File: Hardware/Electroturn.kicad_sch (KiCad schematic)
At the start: 31 parts, among them J1 Encoder Terminal, J2 Stepper Motor Terminal, SW1 Feed Switch, SW2 Motor Braking Switch, SW3 Mode Right Scroll, SW4 Mode Left Scroll, SW5 Function Btn 1, SW6 Function Btn 2, SW7 Function Btn 2, SW8 Control Panel Encoder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

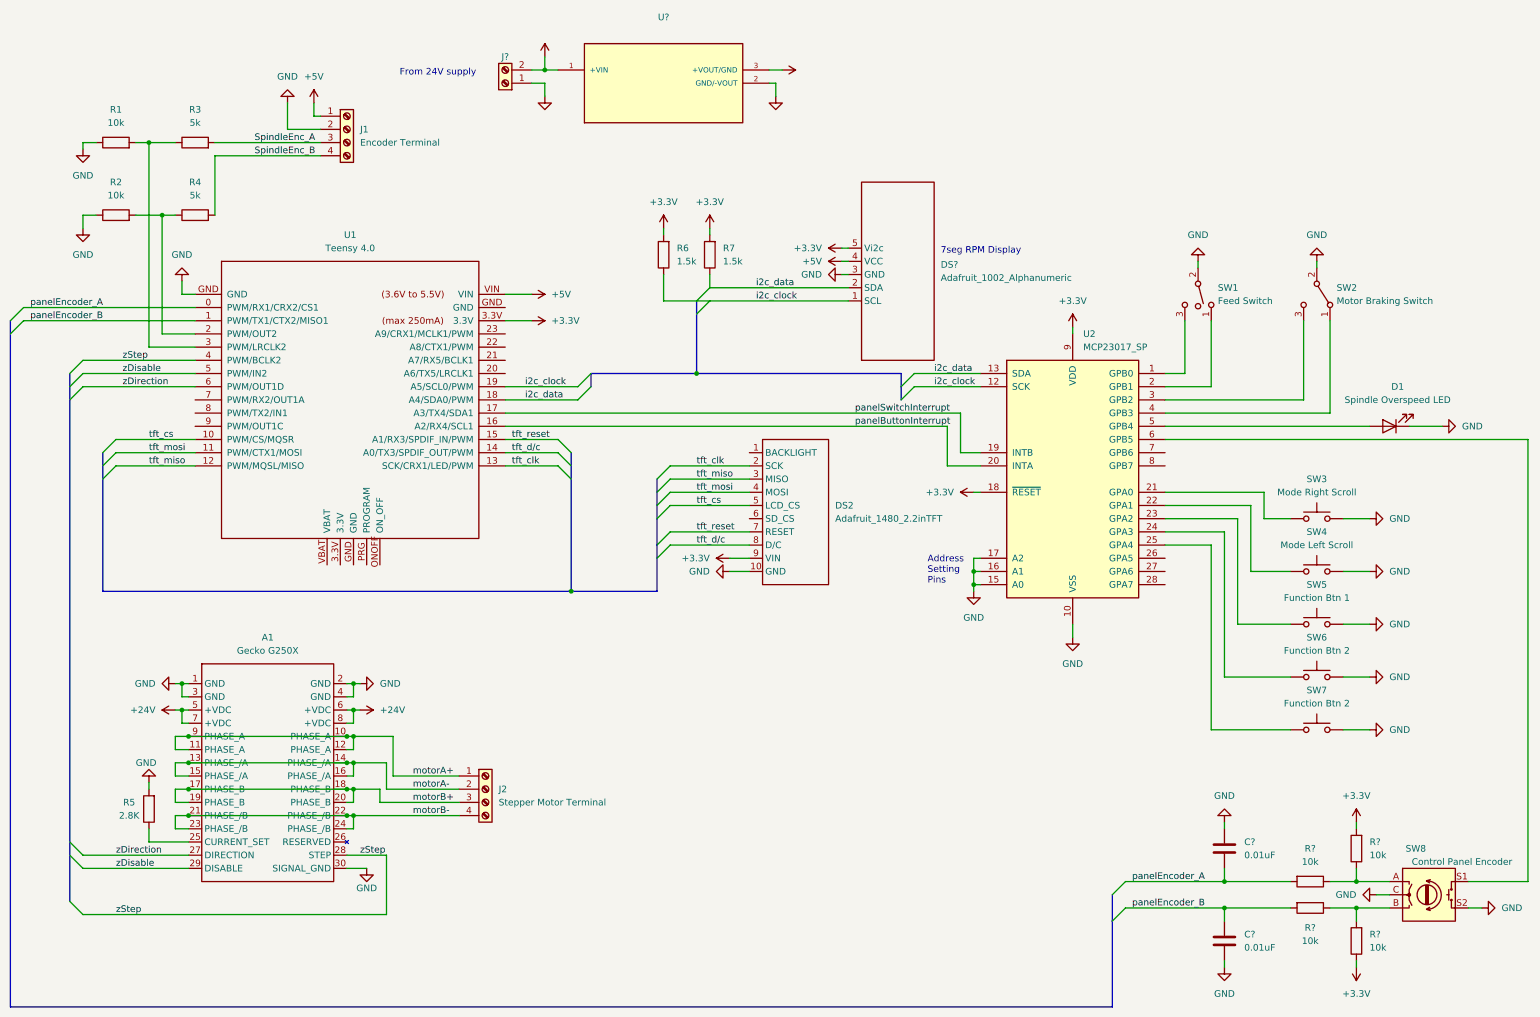
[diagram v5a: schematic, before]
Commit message: Footprint housekeeping, updating PCB components
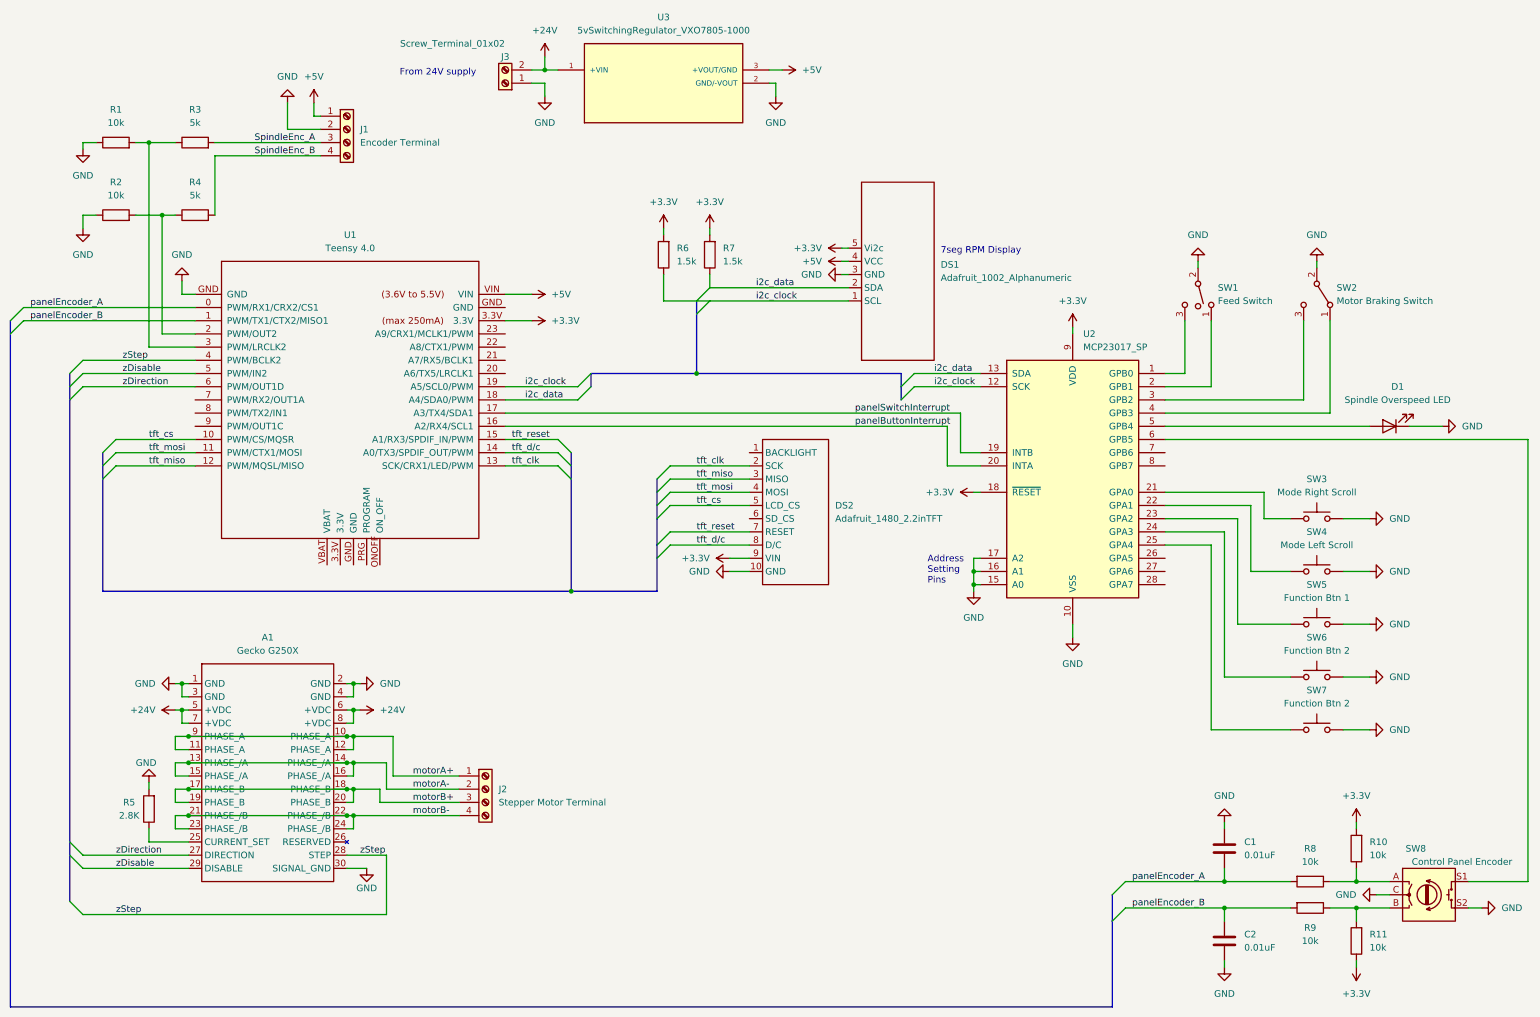
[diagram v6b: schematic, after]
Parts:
- J3: renamed from J?; value (none) -> Screw_Terminal_01x02
- U3: renamed from U?; value (none) -> 5vSwitchingRegulator_VXO7805-1000
- gave numbers to parts that had none: 7

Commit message: Some placement work
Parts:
- C1, C2: footprint (none) -> Capacitor_THT:C_Disc_D6.0mm_W2.5mm_P5.00mm
- D1: footprint (none) -> LED_THT:LED_D5.0mm
- DS1: footprint (none) -> Electroturn_Parts:Adafruit1002_0.54inAlphanumericBackpack
- DS2: footprint (none) -> Electroturn_Parts:Adafruit1480_TFTwithHeaders
- J3: footprint (none) -> Electroturn_Parts:01x02ScrewTerm_OSTVN02A150
- R10, R11, R6, R7, R8, R9: footprint (none) -> Resistor_THT:R_Axial_DIN0411_L9.9mm_D3.6mm_P12.70mm_Horizontal
- SW1: footprint (none) -> Electroturn_Parts:SPDT_OnOffOn_ToggleSwitch_fromECEdepartment_CircularPads
- SW2: footprint (none) -> Electroturn_Parts:SW_SPDT_CK_ A11405RNZQ
- SW3, SW4, SW5, SW6: footprint (none) -> Button_Switch_THT:SW_PUSH_6mm_H9.5mm
- SW7: value Function Btn 2 -> (none); footprint (none) -> Button_Switch_THT:SW_PUSH_6mm_H9.5mm
- SW8: footprint (none) -> Electroturn_Parts:CUIDevices_ACZ11BR1E20FD112C
- U3: footprint (none) -> Electroturn_Parts:5vSwitchingRegulator_CONV_VXO7805-1000
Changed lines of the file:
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@@
     (property "Reference" "SW3" (id 0) (at 303.53 109.22 0))
     (property "Value" "Mode Right Scroll" (id 1) (at 303.53 111.76 0))
-    (property "Footprint" "" (id 2) (at 303.53 111.76 0)
+    (property "Footprint" "Button_Switch_THT:SW_PUSH_6mm_H9.5mm" (id 2) (at 303.53 111.76 0)
       (effects (font (size 1.27 1.27)) hide)
     )
@@
     (property "Reference" "R8" (id 0) (at 302.26 180.34 90))
     (property "Value" "10k" (id 1) (at 302.26 182.88 90))
-    (property "Footprint" "" (id 2) (at 302.26 184.912 90)
+    (property "Footprint" "Resistor_THT:R_Axial_DIN0411_L9.9mm_D3.6mm_P12.70mm_Horizontal" (id 2) (at 302.26 184.912 90)
       (effects (font (size 1.27 1.27)) hide)
     )
@@
     (property "Reference" "SW5" (id 0) (at 303.53 129.54 0))
     (property "Value" "Function Btn 1" (id 1) (at 303.53 132.08 0))
-    (property "Footprint" "" (id 2) (at 303.53 132.08 0)
+    (property "Footprint" "Button_Switch_THT:SW_PUSH_6mm_H9.5mm" (id 2) (at 303.53 132.08 0)
       (effects (font (size 1.27 1.27)) hide)
     )
@@
     (property "Reference" "R9" (id 0) (at 302.26 195.58 90))
     (property "Value" "10k" (id 1) (at 302.26 198.12 90))
-    (property "Footprint" "" (id 2) (at 302.26 189.992 90)
+    (property "Footprint" "Resistor_THT:R_Axial_DIN0411_L9.9mm_D3.6mm_P12.70mm_Horizontal" (id 2) (at 302.26 189.992 90)
       (effects (font (size 1.27 1.27)) hide)
     )
@@
     (property "Reference" "J3" (id 0) (at 147.32 27.94 0))
     (property "Value" "Screw_Terminal_01x02" (id 1) (at 137.16 25.4 0))
-    (property "Footprint" "" (id 2) (at 147.32 33.02 0)
+    (property "Footprint" "Electroturn_Parts:01x02ScrewTerm_OSTVN02A150" (id 2) (at 147.32 33.02 0)
       (effects (font (size 1.27 1.27)) hide)
     )
@@
     (property "Reference" "SW4" (id 0) (at 303.53 119.38 0))
     (property "Value" "Mode Left Scroll" (id 1) (at 303.53 121.92 0))
-    (property "Footprint" "" (id 2) (at 303.53 121.92 0)
+    (property "Footprint" "Button_Switch_THT:SW_PUSH_6mm_H9.5mm" (id 2) (at 303.53 121.92 0)
       (effects (font (size 1.27 1.27)) hide)
     )
@@
       (effects (font (size 1.27 1.27)) (justify left))
     )
-    (property "Footprint" "" (id 2) (at 286.7152 184.15 0)
+    (property "Footprint" "Capacitor_THT:C_Disc_D6.0mm_W2.5mm_P5.00mm" (id 2) (at 286.7152 184.15 0)
       (effects (font (size 1.27 1.27)) hide)
     )
@@
     (property "Reference" "SW6" (id 0) (at 303.53 139.7 0))
     (property "Value" "Function Btn 2" (id 1) (at 303.53 142.24 0))
-    (property "Footprint" "" (id 2) (at 303.53 142.24 0)
+    (property "Footprint" "Button_Switch_THT:SW_PUSH_6mm_H9.5mm" (id 2) (at 303.53 142.24 0)
       (effects (font (size 1.27 1.27)) hide)
     )
@@
       (effects (font (size 1.27 1.27)) (justify left))
     )
-    (property "Footprint" "" (id 2) (at 303.53 73.66 0)
+    (property "Footprint" "Electroturn_Parts:SW_SPDT_CK_ A11405RNZQ" (id 2) (at 303.53 73.66 0)
       (effects (font (size 1.27 1.27)) hide)
     )
@@
       (effects (font (size 1.27 1.27)) (justify right))
     )
-    (property "Footprint" "" (id 2) (at 312.928 198.12 90)
+    (property "Footprint" "Resistor_THT:R_Axial_DIN0411_L9.9mm_D3.6mm_P12.70mm_Horizontal" (id 2) (at 312.928 198.12 90)
       (effects (font (size 1.27 1.27)) hide)
     )
@@
       (effects (font (size 1.27 1.27)) (justify left))
     )
-    (property "Footprint" "" (id 2) (at 210.82 134.62 0)
+    (property "Footprint" "Electroturn_Parts:Adafruit1480_TFTwithHeaders" (id 2) (at 210.82 134.62 0)
       (effects (font (size 1.27 1.27)) hide)
     )
@@
       (effects (font (size 1.27 1.27)) (justify left))
     )
-    (property "Footprint" "" (id 2) (at 286.7152 201.93 0)
+    (property "Footprint" "Capacitor_THT:C_Disc_D6.0mm_W2.5mm_P5.00mm" (id 2) (at 286.7152 201.93 0)
       (effects (font (size 1.27 1.27)) hide)
     )
@@
     (property "Reference" "SW8" (id 0) (at 322.58 180.34 0))
     (property "Value" "Control Panel Encoder" (id 1) (at 331.47 182.88 0))
-    (property "Footprint" "" (id 2) (at 321.31 185.166 0)
+    (property "Footprint" "Electroturn_Parts:CUIDevices_ACZ11BR1E20FD112C" (id 2) (at 321.31 185.166 0)
       (effects (font (size 1.27 1.27)) hide)
     )
@@
       (effects (font (size 1.27 1.27)) (justify right))
     )
-    (property "Footprint" "" (id 2) (at 188.468 66.04 90)
+    (property "Footprint" "Resistor_THT:R_Axial_DIN0411_L9.9mm_D3.6mm_P12.70mm_Horizontal" (id 2) (at 188.468 66.04 90)
       (effects (font (size 1.27 1.27)) hide)
     )
@@
       (effects (font (size 1.27 1.27)) (justify right))
     )
-    (property "Footprint" "" (id 2) (at 312.928 180.34 90)
+    (property "Footprint" "Resistor_THT:R_Axial_DIN0411_L9.9mm_D3.6mm_P12.70mm_Horizontal" (id 2) (at 312.928 180.34 90)
       (effects (font (size 1.27 1.27)) hide)
     )
@@
     (property "Reference" "U3" (id 0) (at 177.8 20.32 0))
     (property "Value" "5vSwitchingRegulator_VXO7805-1000" (id 1) (at 177.8 22.86 0))
-    (property "Footprint" "" (id 2) (at 162.56 52.07 0)
+    (property "Footprint" "Electroturn_Parts:5vSwitchingRegulator_CONV_VXO7805-1000" (id 2) (at 162.56 52.07 0)
       (effects (font (size 1.27 1.27)) (justify left bottom) hide)
     )
@@
       (effects (font (size 1.27 1.27)) (justify right))
     )
-    (property "Footprint" "" (id 2) (at 223.52 69.85 0)
+    (property "Footprint" "Electroturn_Parts:Adafruit1002_0.54inAlphanumericBackpack" (id 2) (at 223.52 69.85 0)
       (effects (font (size 1.27 1.27)) hide)
     )
@@
     (in_bom yes) (on_board yes) (fields_autoplaced)
     (property "Reference" "SW7" (id 0) (at 303.53 149.86 0))
-    (property "Value" "Function Btn 2" (id 1) (at 303.53 152.4 0))
-    (property "Footprint" "" (id 2) (at 303.53 152.4 0)
+    (property "Value" "" (id 1) (at 303.53 152.4 0))
+    (property "Footprint" "Button_Switch_THT:SW_PUSH_6mm_H9.5mm" (id 2) (at 303.53 152.4 0)
       (effects (font (size 1.27 1.27)) hide)
     )
@@
       (effects (font (size 1.27 1.27)) (justify left))
     )
-    (property "Footprint" "" (id 2) (at 280.67 73.66 0)
+    (property "Footprint" "Electroturn_Parts:SPDT_OnOffOn_ToggleSwitch_fromECEdepartment_CircularPads" (id 2) (at 280.67 73.66 0)
       (effects (font (size 1.27 1.27)) hide)
     )
@@
       (effects (font (size 1.27 1.27)) (justify right))
     )
-    (property "Footprint" "" (id 2) (at 179.578 66.04 90)
+    (property "Footprint" "Resistor_THT:R_Axial_DIN0411_L9.9mm_D3.6mm_P12.70mm_Horizontal" (id 2) (at 179.578 66.04 90)
       (effects (font (size 1.27 1.27)) hide)
     )
@@
     (property "Reference" "D1" (id 0) (at 319.0875 91.44 0))
     (property "Value" "Spindle Overspeed LED" (id 1) (at 319.0875 93.98 0))
-    (property "Footprint" "" (id 2) (at 317.5 99.06 0)
+    (property "Footprint" "LED_THT:LED_D5.0mm" (id 2) (at 317.5 99.06 0)
       (effects (font (size 1.27 1.27)) hide)
     )
@@
     )
     (path "/a8a94bfd-35ac-45a8-aada-ab5c5fe749d7"
-      (reference "SW7") (unit 1) (value "Function Btn 2") (footprint "Button_Switch_THT:SW_PUSH_6mm_H9.5mm")
+      (reference "SW7") (unit 1) (value "Function Btn 3") (footprint "Button_Switch_THT:SW_PUSH_6mm_H9.5mm")
     )
     (path "/634f1bbf-7356-47c8-8fb1-56a0c758ceaa"

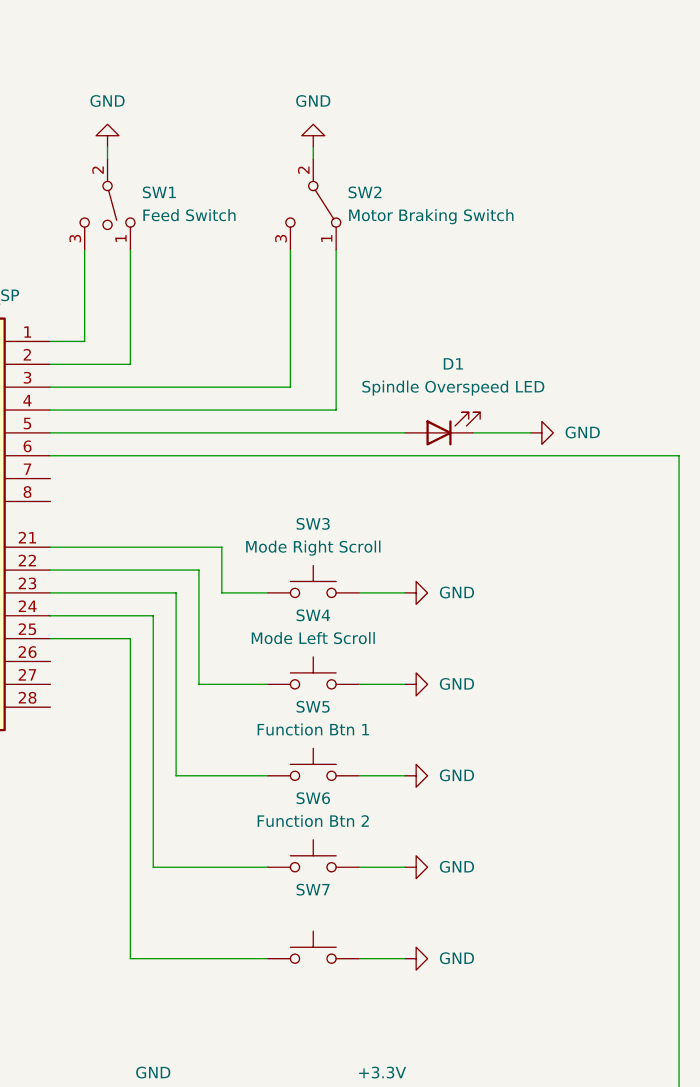
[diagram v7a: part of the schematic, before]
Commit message: Fixing schematic parity issues with PCB footprints
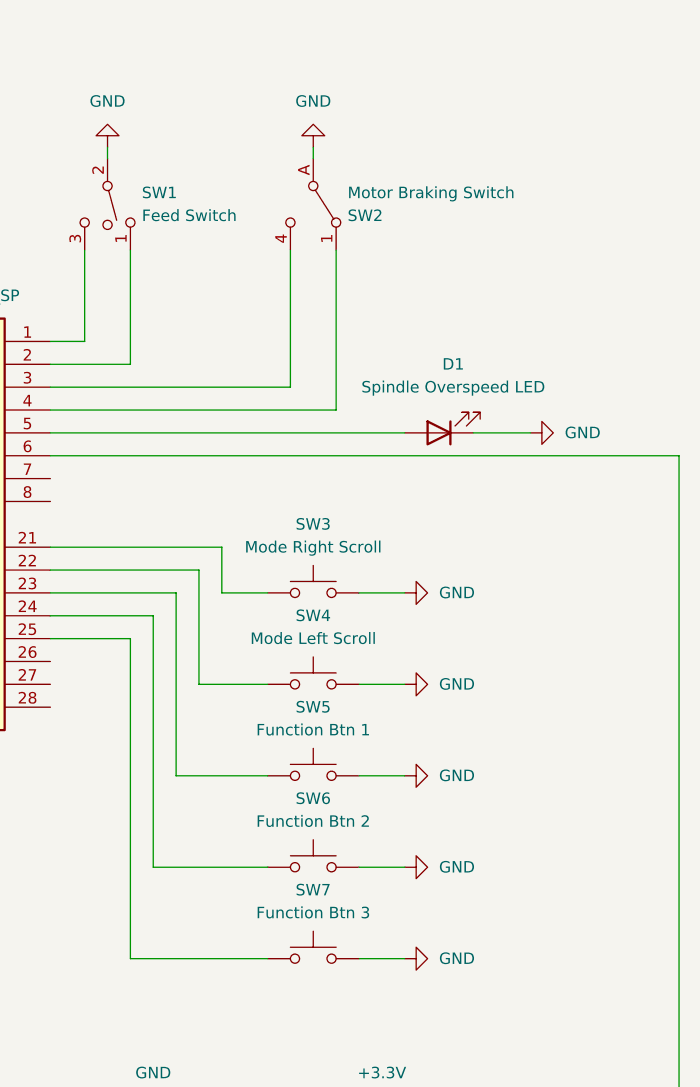
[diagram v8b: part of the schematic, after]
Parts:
- SW7: value (none) -> Function Btn 3
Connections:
- net GND: now also SW2.A; no longer SW2.2 (B)
- net at U2.3 (GPB2): now also SW2.4; no longer SW2.3 (C)
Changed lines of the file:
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@@
   )
   (symbol (lib_id "Switch:SW_SPDT") (at 303.53 73.66 270) (unit 1)
-    (in_bom yes) (on_board yes) (fields_autoplaced)
-    (property "Reference" "SW2" (id 0) (at 307.34 72.3899 90)
-      (effects (font (size 1.27 1.27)) (justify left))
-    )
-    (property "Value" "Motor Braking Switch" (id 1) (at 307.34 74.9299 90)
+    (in_bom yes) (on_board yes)
+    (property "Reference" "SW2" (id 0) (at 307.34 74.93 90)
+      (effects (font (size 1.27 1.27)) (justify left))
+    )
+    (property "Value" "Motor Braking Switch" (id 1) (at 307.34 72.39 90)
       (effects (font (size 1.27 1.27)) (justify left))
     )
@@
     )
     (pin "1")
-    (pin "2")
-    (pin "3")
+    (pin "A")
+    (pin "4")
   )
   (symbol (lib_id "Device:R") (at 311.15 198.12 180) (unit 1)
@@
     (in_bom yes) (on_board yes) (fields_autoplaced)
     (property "Reference" "SW7" (id 0) (at 303.53 149.86 0))
-    (property "Value" "" (id 1) (at 303.53 152.4 0))
+    (property "Value" "Function Btn 3" (id 1) (at 303.53 152.4 0))
     (property "Footprint" "Button_Switch_THT:SW_PUSH_6mm_H9.5mm" (id 2) (at 303.53 152.4 0)
       (effects (font (size 1.27 1.27)) hide)
